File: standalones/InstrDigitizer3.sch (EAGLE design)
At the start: 78 parts, among them Q1 310mA/60V/1.6Ω, Q4 MOSFET-NCH-AO3404A, Q5 MOSFET-NCH-AO3404A, U1 LTC2251, U2 MCP4725, U3 LT5560, U4 MCP1703CB, U5 MCP4725

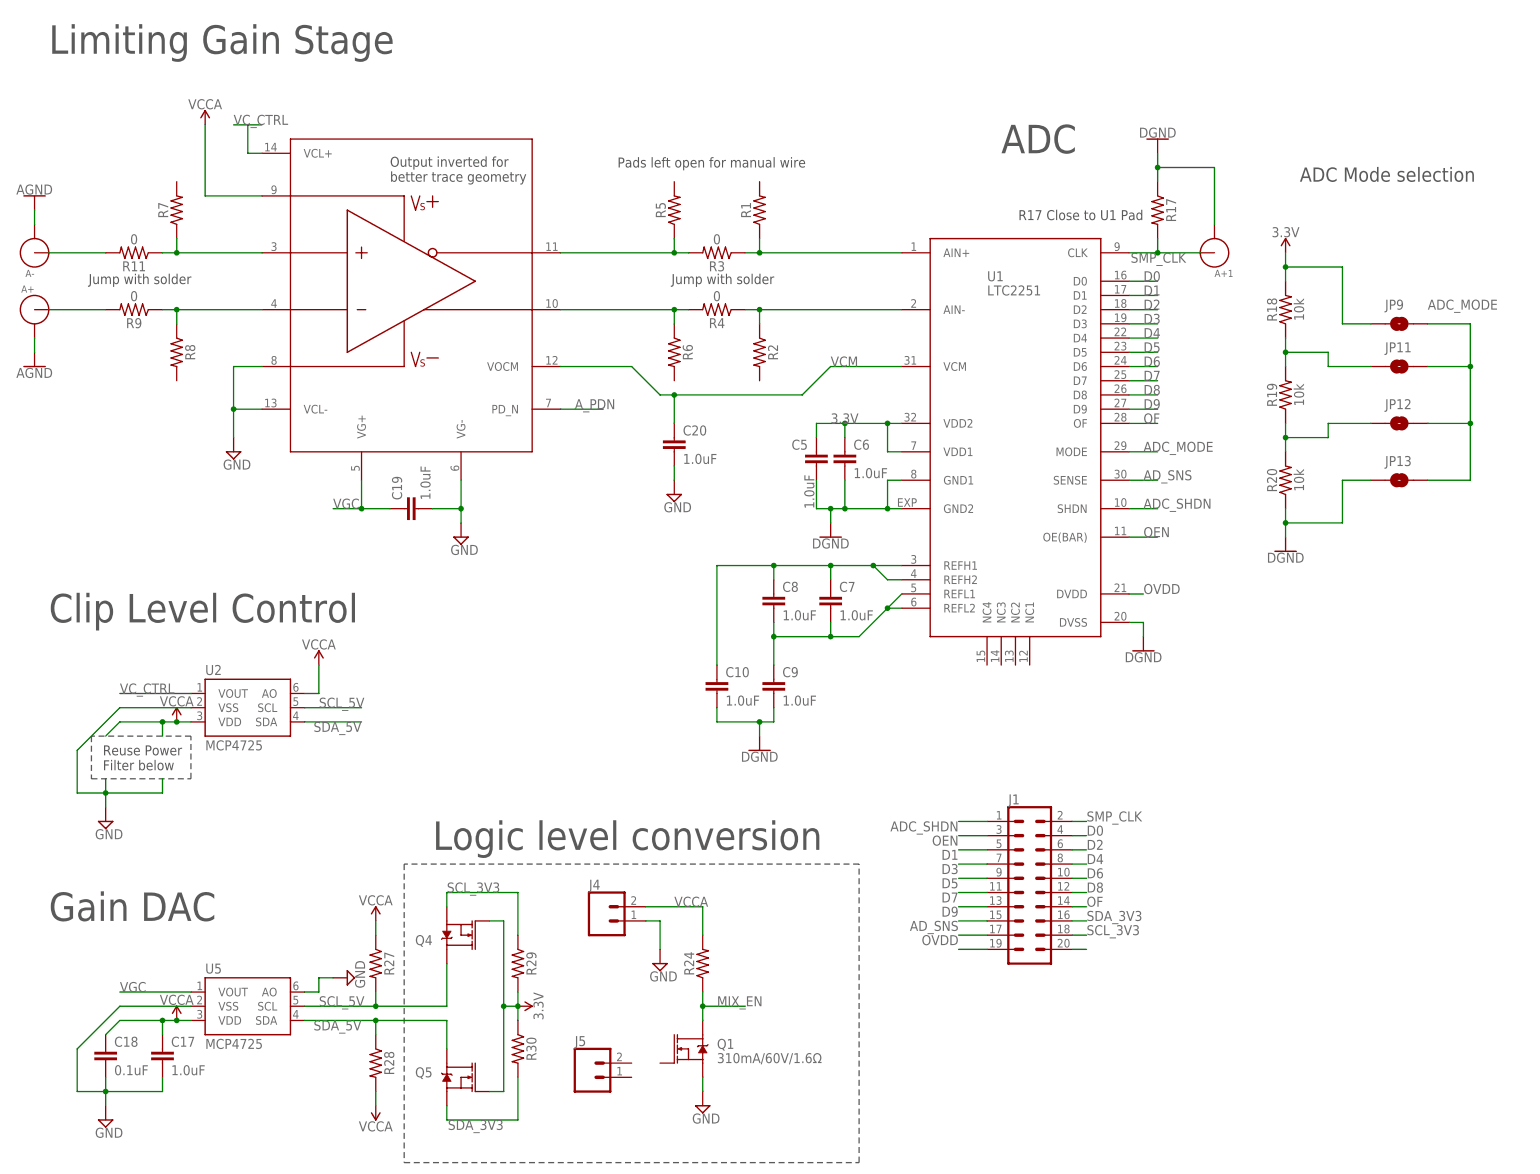
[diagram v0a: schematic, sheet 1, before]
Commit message: New board in Standalones, InstrDigitizer(4/5)
added new parts with old ADC and capability to break away individual ICs.
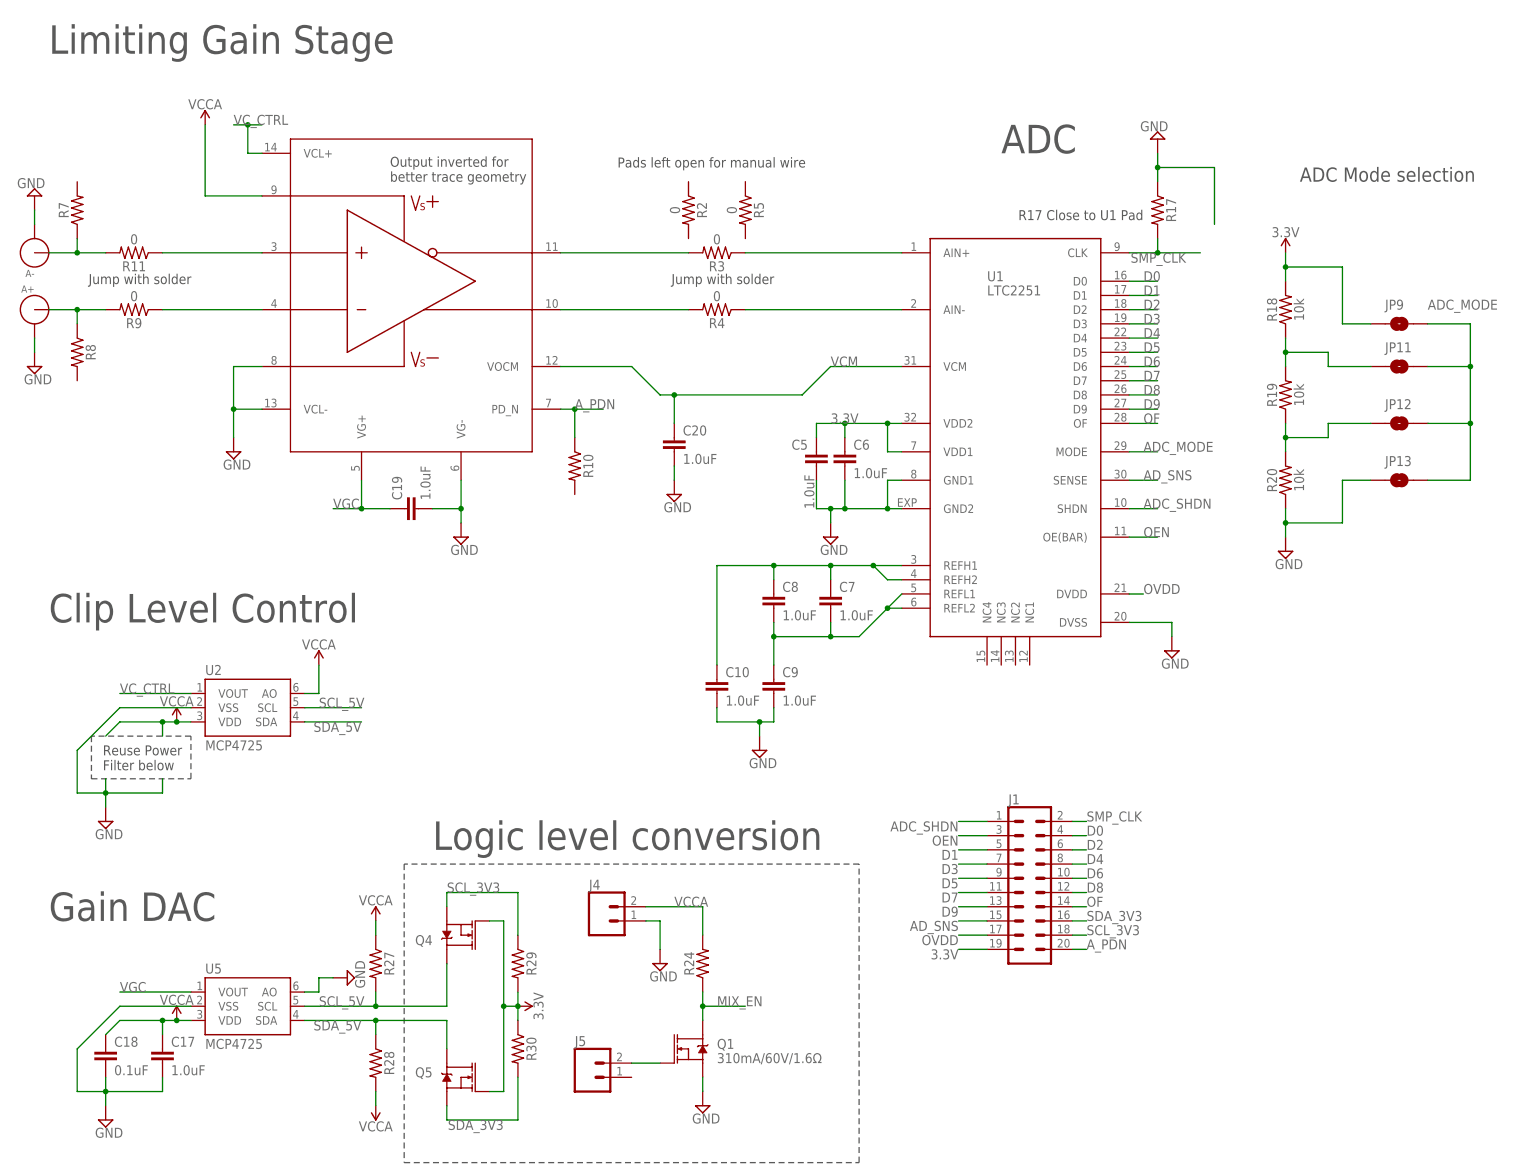
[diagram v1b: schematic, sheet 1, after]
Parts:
- removed A+1: LINX-SMA-EDGE-0.062, connector:LINX-SMA-EDGE-0.062
- removed R1, R21, R22, R6: (no value), SparkFun-Resistors:RESISTOR0402
- added J2: (no value), SparkFun-Connectors:JST_2MM_MALE
- added R10: (no value), SparkFun-Resistors:RESISTOR0402
- R2, R5: value (none) -> 0
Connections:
- removed net N$8: J1.20
- removed net N$9: J1.19
- new net N$3: J5.2, Q1.G
- net 3.3V: now also J1.19
- net A_PDN: now also J1.20, R10.1
- net GND: now also J2.-; no longer A+1.P$2, R21.1, R21.2, R22.1, R22.2
- net N$1: no longer R7.1
- net N$10: now also R7.1
- net N$11: no longer R8.1
- net N$2: now also R8.1
- net N$4: no longer R1.1
- net N$5: no longer R5.1
- net N$6: no longer R2.1
- net N$7: no longer R6.1
- net SMP_CLK: no longer A+1.ANT
- net VCCA: now also J2.+
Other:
- moved on the sheet: J3, R2, R5, R7, R8
